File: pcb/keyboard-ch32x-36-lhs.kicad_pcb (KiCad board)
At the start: 2 copper layers, 100 x 96.5 mm, 57 parts, among them J1 USB Type-C Receptacle 12-pin, J2 PJ-320A, J4 Conn_01x02, J5 Conn_01x03, SW1 SW_SPST, SW2 SW_SPST, U1 CH32X033F8P6

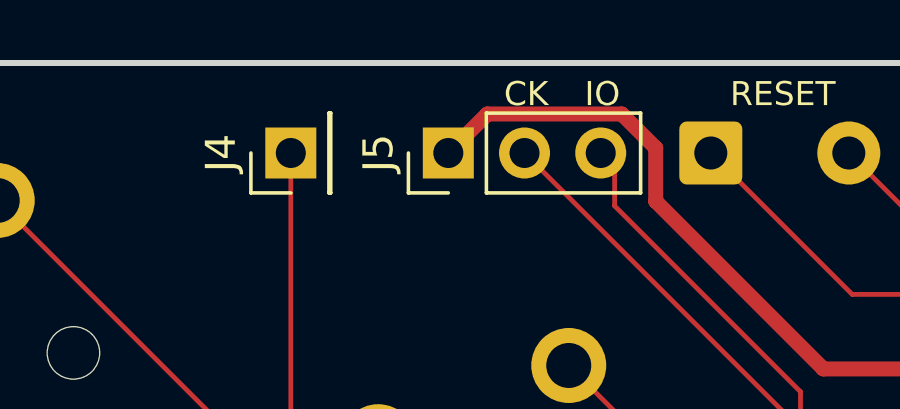
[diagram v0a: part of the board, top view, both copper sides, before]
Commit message: pcb: ch32x-36-lhs: add SilkScr "G" to SWD
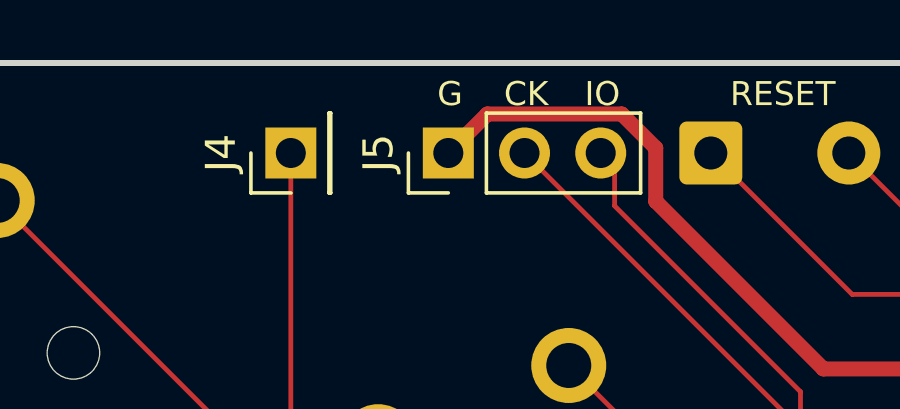
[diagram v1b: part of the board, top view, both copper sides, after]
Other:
- board text added: "G"
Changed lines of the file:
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@@
+		)
+	)
+	(gr_text "G"
+		(at 162.306 51.5 0)
+		(layer "F.SilkS")
+		(effects
+			(font
+				(size 0.8 0.8)
+				(thickness 0.15)
+			)
+			(justify bottom)
 		)
 	)
